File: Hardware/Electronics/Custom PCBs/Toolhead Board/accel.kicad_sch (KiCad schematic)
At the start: 1 part, among them U10 BMI270

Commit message: Remove locks
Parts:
- added C49: 100n, symbol Device:C
- added JP2: SolderJumper_3_Bridged123, symbol Jumper:SolderJumper_3_Bridged123
- added JP3: SolderJumper_2_Open, symbol Jumper:SolderJumper_2_Open
- added R39, R40: 2.2k, symbol Device:R
- added R41: 10k, symbol Device:R
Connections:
- net Address Selection: now reaches U10.1 (SDO)
- net Address Selection: now also JP3.2 (B), R41.1
- net SCL: now reaches U10.13 (SCX)
- net SCL: now also R39.2
- net SDA: now reaches U10.14 (SDX)
- net SDA: now also R40.2
- net +3.3V: now reaches U10.5 (VDDIO)
- net +3.3V: now also U10.8 (VDD), C49.1, JP2.2 (C), JP3.1 (A)
- net GND: now reaches U10.6 (GNDIO)
- net GND: now also U10.7 (GND), C49.2, R41.2
- new net: JP2.1 (A), R39.1
- new net: JP2.3 (B), R40.1
- no-connect marks 0 -> 7
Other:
- moved on the sheet: U10

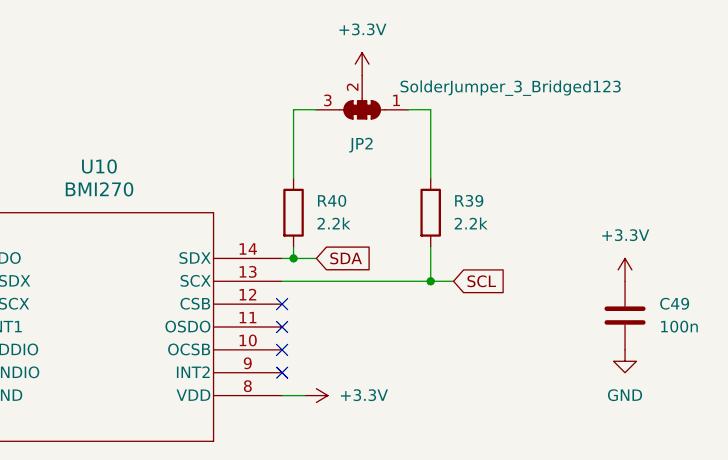
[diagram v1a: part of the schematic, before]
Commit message: Finish Toolhead Schematic
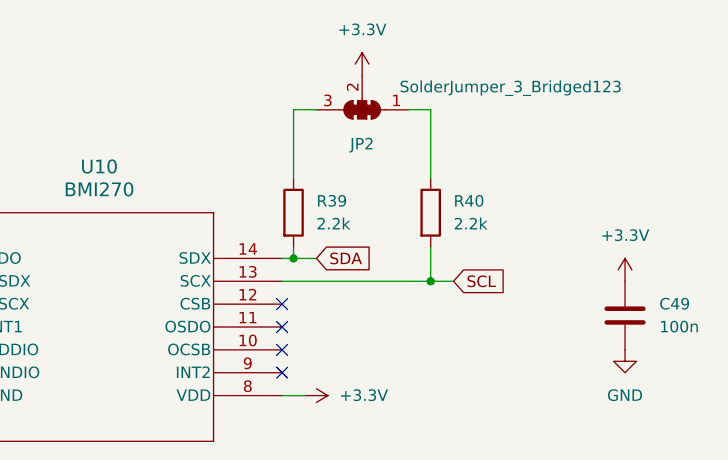
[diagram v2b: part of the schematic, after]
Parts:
- C49: Digikey (none) -> 1276-1935-1-ND
- R39: renamed from R40; footprint (none) -> Resistor_SMD:R_0603_1608Metric_Pad0.98x0.95mm_HandSolder; Digikey (none) -> 1292-WR06X103JTLCT-ND
- R40: renamed from R39; footprint (none) -> Resistor_SMD:R_0603_1608Metric_Pad0.98x0.95mm_HandSolder; Digikey (none) -> 1292-WR06X103JTLCT-ND
- R41: footprint (none) -> Resistor_SMD:R_0603_1608Metric_Pad0.98x0.95mm_HandSolder; Digikey (none) -> 1292-WR06X103JTLCT-ND
- U10: Digikey (none) -> 828-1091-1-ND
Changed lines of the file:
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@@
   (symbol (lib_id "power:GND") (at 59.69 58.42 270) (unit 1)
     (in_bom yes) (on_board yes) (dnp no) (fields_autoplaced)
-    (property "Reference" "#PWR074" (at 53.34 58.42 0)
+    (property "Reference" "#PWR099" (at 53.34 58.42 0)
       (effects (font (size 1.27 1.27)) hide)
     )
@@
       (project "Toolhead Board"
         (path "/a1747683-152e-4245-ab61-2d33ce6021ef/7be2b1b8-8861-4283-9878-3fb2e6cb9107"
-          (reference "#PWR074") (unit 1)
+          (reference "#PWR099") (unit 1)
         )
       )
@@
       (effects (font (size 1.27 1.27)) hide)
     )
+    (property "Digikey" "1276-1935-1-ND" (at 140.97 49.53 0)
+      (effects (font (size 1.27 1.27)) hide)
+    )
     (pin "1")
     (pin "2")
@@
     (property "Datasheet" "BMI270" (at 62.23 43.18 0)
       (effects (font (size 1.27 1.27) italic) hide)
+    )
+    (property "Digikey" "828-1091-1-ND" (at 62.23 43.18 0)
+      (effects (font (size 1.27 1.27)) hide)
     )
     (pin "1")
@@
     (pin "4")
     (pin "5")
+    (pin "8")
+    (pin "9")
     (pin "6")
     (pin "7")
-    (pin "8")
-    (pin "9")
     (instances
       (project "Toolhead Board"
@@
   (symbol (lib_id "Device:R") (at 119.38 38.1 0) (unit 1)
     (in_bom yes) (on_board yes) (dnp no) (fields_autoplaced)
-    (property "Reference" "R39" (at 121.92 36.83 0)
+    (property "Reference" "R40" (at 121.92 36.83 0)
       (effects (font (size 1.27 1.27)) (justify left))
     )
@@
       (effects (font (size 1.27 1.27)) (justify left))
     )
-    (property "Footprint" "" (at 117.602 38.1 90)
+    (property "Footprint" "Resistor_SMD:R_0603_1608Metric_Pad0.98x0.95mm_HandSolder" (at 117.602 38.1 90)
       (effects (font (size 1.27 1.27)) hide)
     )
@@
       (effects (font (size 1.27 1.27)) hide)
     )
-    (pin "1")
-    (pin "2")
-    (instances
-      (project "Toolhead Board"
-        (path "/a1747683-152e-4245-ab61-2d33ce6021ef/7be2b1b8-8861-4283-9878-3fb2e6cb9107"
-          (reference "R39") (unit 1)
+    (property "Digikey" "1292-WR06X103JTLCT-ND" (at 119.38 38.1 0)
+      (effects (font (size 1.27 1.27)) hide)
+    )
+    (pin "1")
+    (pin "2")
+    (instances
+      (project "Toolhead Board"
+        (path "/a1747683-152e-4245-ab61-2d33ce6021ef/7be2b1b8-8861-4283-9878-3fb2e6cb9107"
+          (reference "R40") (unit 1)
         )
       )
@@
   (symbol (lib_id "power:+3.3V") (at 41.91 35.56 0) (unit 1)
     (in_bom yes) (on_board yes) (dnp no) (fields_autoplaced)
-    (property "Reference" "#PWR079" (at 41.91 39.37 0)
+    (property "Reference" "#PWR094" (at 41.91 39.37 0)
       (effects (font (size 1.27 1.27)) hide)
     )
@@
       (project "Toolhead Board"
         (path "/a1747683-152e-4245-ab61-2d33ce6021ef/7be2b1b8-8861-4283-9878-3fb2e6cb9107"
-          (reference "#PWR079") (unit 1)
+          (reference "#PWR094") (unit 1)
         )
       )
@@
       (effects (font (size 1.27 1.27)) (justify left))
     )
-    (property "Footprint" "" (at 43.688 46.99 90)
+    (property "Footprint" "Resistor_SMD:R_0603_1608Metric_Pad0.98x0.95mm_HandSolder" (at 43.688 46.99 90)
       (effects (font (size 1.27 1.27)) hide)
     )
@@
       (effects (font (size 1.27 1.27)) hide)
     )
+    (property "Digikey" "1292-WR06X103JTLCT-ND" (at 41.91 46.99 0)
+      (effects (font (size 1.27 1.27)) hide)
+    )
     (pin "1")
     (pin "2")
@@
   (symbol (lib_id "power:+3.3V") (at 140.97 45.72 0) (unit 1)
     (in_bom yes) (on_board yes) (dnp no) (fields_autoplaced)
-    (property "Reference" "#PWR077" (at 140.97 49.53 0)
+    (property "Reference" "#PWR095" (at 140.97 49.53 0)
       (effects (font (size 1.27 1.27)) hide)
     )
@@
       (project "Toolhead Board"
         (path "/a1747683-152e-4245-ab61-2d33ce6021ef/7be2b1b8-8861-4283-9878-3fb2e6cb9107"
-          (reference "#PWR077") (unit 1)
+          (reference "#PWR095") (unit 1)
         )
       )
@@
   (symbol (lib_id "power:+3.3V") (at 105.41 58.42 270) (unit 1)
     (in_bom yes) (on_board yes) (dnp no) (fields_autoplaced)
-    (property "Reference" "#PWR076" (at 101.6 58.42 0)
+    (property "Reference" "#PWR0100" (at 101.6 58.42 0)
       (effects (font (size 1.27 1.27)) hide)
     )
@@
       (project "Toolhead Board"
         (path "/a1747683-152e-4245-ab61-2d33ce6021ef/7be2b1b8-8861-4283-9878-3fb2e6cb9107"
-          (reference "#PWR076") (unit 1)
+          (reference "#PWR0100") (unit 1)
         )
       )
@@
   (symbol (lib_id "power:+3.3V") (at 59.69 53.34 90) (unit 1)
     (in_bom yes) (on_board yes) (dnp no) (fields_autoplaced)
-    (property "Reference" "#PWR075" (at 63.5 53.34 0)
+    (property "Reference" "#PWR097" (at 63.5 53.34 0)
       (effects (font (size 1.27 1.27)) hide)
     )
@@
       (project "Toolhead Board"
         (path "/a1747683-152e-4245-ab61-2d33ce6021ef/7be2b1b8-8861-4283-9878-3fb2e6cb9107"
-          (reference "#PWR075") (unit 1)
+          (reference "#PWR097") (unit 1)
         )
       )
@@
   (symbol (lib_id "power:GND") (at 41.91 50.8 0) (unit 1)
     (in_bom yes) (on_board yes) (dnp no) (fields_autoplaced)
-    (property "Reference" "#PWR080" (at 41.91 57.15 0)
+    (property "Reference" "#PWR096" (at 41.91 57.15 0)
       (effects (font (size 1.27 1.27)) hide)
     )
@@
       (project "Toolhead Board"
         (path "/a1747683-152e-4245-ab61-2d33ce6021ef/7be2b1b8-8861-4283-9878-3fb2e6cb9107"
-          (reference "#PWR080") (unit 1)
+          (reference "#PWR096") (unit 1)
         )
       )
@@
   (symbol (lib_id "Device:R") (at 104.14 38.1 0) (unit 1)
     (in_bom yes) (on_board yes) (dnp no) (fields_autoplaced)
-    (property "Reference" "R40" (at 106.68 36.83 0)
+    (property "Reference" "R39" (at 106.68 36.83 0)
       (effects (font (size 1.27 1.27)) (justify left))
     )
@@
       (effects (font (size 1.27 1.27)) (justify left))
     )
-    (property "Footprint" "" (at 102.362 38.1 90)
+    (property "Footprint" "Resistor_SMD:R_0603_1608Metric_Pad0.98x0.95mm_HandSolder" (at 102.362 38.1 90)
       (effects (font (size 1.27 1.27)) hide)
     )
@@
       (effects (font (size 1.27 1.27)) hide)
     )
-    (pin "1")
-    (pin "2")
-    (instances
-      (project "Toolhead Board"
-        (path "/a1747683-152e-4245-ab61-2d33ce6021ef/7be2b1b8-8861-4283-9878-3fb2e6cb9107"
-          (reference "R40") (unit 1)
+    (property "Digikey" "1292-WR06X103JTLCT-ND" (at 104.14 38.1 0)
+      (effects (font (size 1.27 1.27)) hide)
+    )
+    (pin "1")
+    (pin "2")
+    (instances
+      (project "Toolhead Board"
+        (path "/a1747683-152e-4245-ab61-2d33ce6021ef/7be2b1b8-8861-4283-9878-3fb2e6cb9107"
+          (reference "R39") (unit 1)
         )
       )
@@
   (symbol (lib_id "power:GND") (at 140.97 53.34 0) (unit 1)
     (in_bom yes) (on_board yes) (dnp no) (fields_autoplaced)
-    (property "Reference" "#PWR078" (at 140.97 59.69 0)
+    (property "Reference" "#PWR098" (at 140.97 59.69 0)
       (effects (font (size 1.27 1.27)) hide)
     )
@@
       (project "Toolhead Board"
         (path "/a1747683-152e-4245-ab61-2d33ce6021ef/7be2b1b8-8861-4283-9878-3fb2e6cb9107"
-          (reference "#PWR078") (unit 1)
+          (reference "#PWR098") (unit 1)
         )
       )
@@
   (symbol (lib_id "power:+3.3V") (at 111.76 22.86 0) (unit 1)
     (in_bom yes) (on_board yes) (dnp no) (fields_autoplaced)
-    (property "Reference" "#PWR073" (at 111.76 26.67 0)
+    (property "Reference" "#PWR093" (at 111.76 26.67 0)
       (effects (font (size 1.27 1.27)) hide)
     )
@@
       (project "Toolhead Board"
         (path "/a1747683-152e-4245-ab61-2d33ce6021ef/7be2b1b8-8861-4283-9878-3fb2e6cb9107"
-          (reference "#PWR073") (unit 1)
-        )
-      )
+          (reference "#PWR093") (unit 1)
+        )
+      )

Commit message: Continue adding footprints
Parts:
- C49: footprint (none) -> Capacitor_SMD:C_0603_1608Metric_Pad1.08x0.95mm_HandSolder
- JP2: footprint (none) -> Jumper:SolderJumper-3_P1.3mm_Open_RoundedPad1.0x1.5mm
- JP3: footprint (none) -> Jumper:SolderJumper-2_P1.3mm_Open_RoundedPad1.0x1.5mm
- U10: footprint BMI270_BOS -> Package_LGA:Bosch_LGA-14_3x2.5mm_P0.5mm
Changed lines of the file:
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@@
 			)
 		)
-		(property "Footprint" ""
+		(property "Footprint" "Jumper:SolderJumper-3_P1.3mm_Open_RoundedPad1.0x1.5mm"
 			(at 111.76 26.67 0)
 			(effects
@@
 			)
 		)
-		(property "Footprint" ""
+		(property "Footprint" "Jumper:SolderJumper-2_P1.3mm_Open_RoundedPad1.0x1.5mm"
 			(at 41.91 39.37 0)
 			(effects
@@
 			)
 		)
-		(property "Footprint" ""
+		(property "Footprint" "Capacitor_SMD:C_0603_1608Metric_Pad1.08x0.95mm_HandSolder"
 			(at 141.9352 53.34 0)
 			(effects
@@
 			)
 		)
-		(property "Footprint" "BMI270_BOS"
+		(property "Footprint" "Package_LGA:Bosch_LGA-14_3x2.5mm_P0.5mm"
 			(at 62.23 43.18 0)
 			(effects

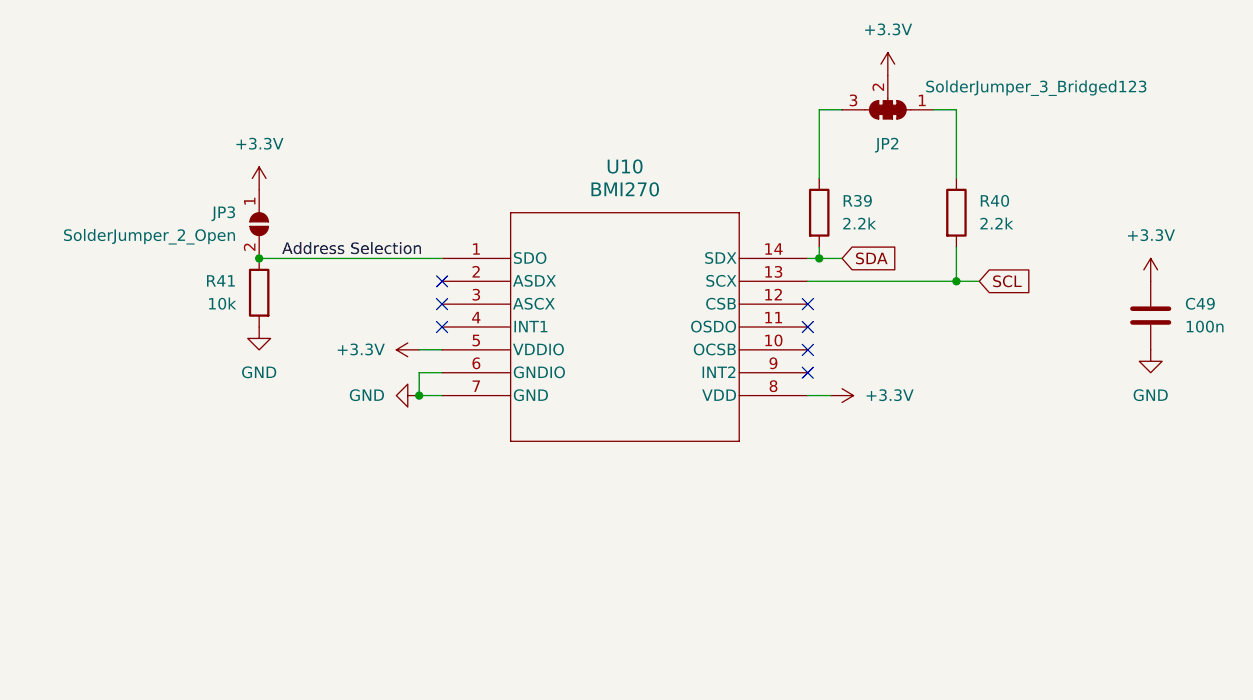
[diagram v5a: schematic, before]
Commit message: Update toolhead schematic+layout and add tolerances to base
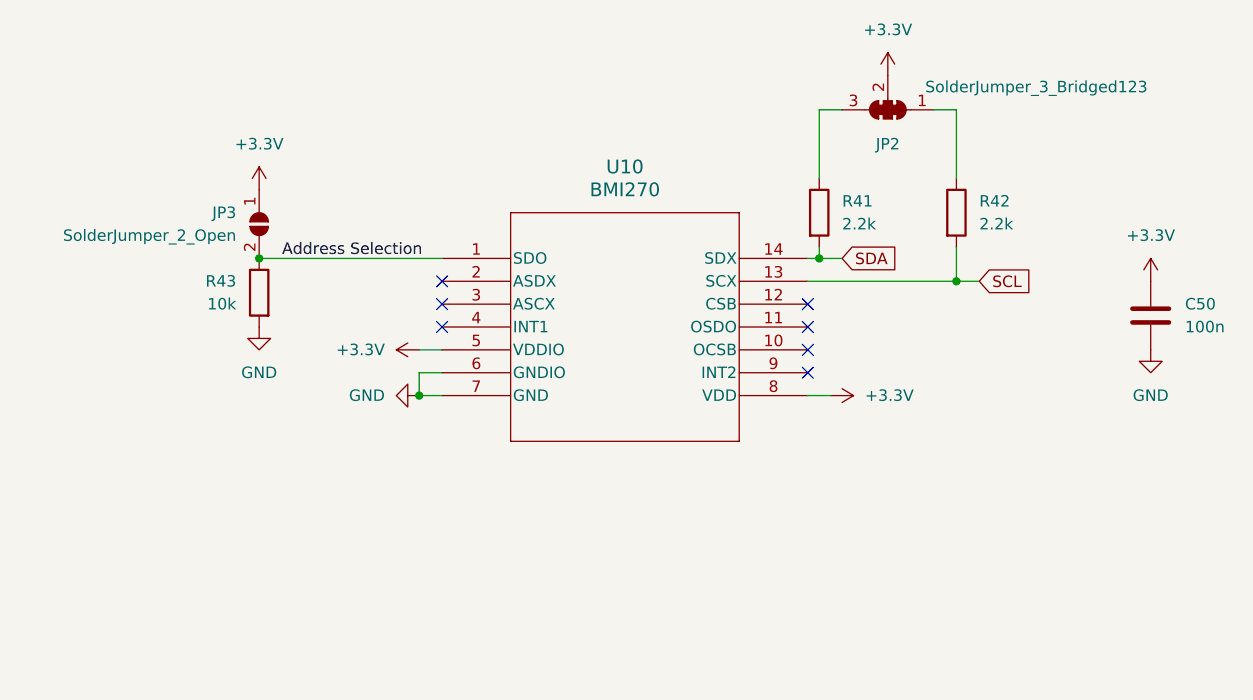
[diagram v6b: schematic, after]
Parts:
- renumbered C49 to C50, R39 to R41, R40 to R42, R41 to R43
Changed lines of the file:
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@@
 		(dnp no)
 		(fields_autoplaced yes)
-		(property "Reference" "#PWR098"
+		(property "Reference" "#PWR0100"
 			(at 53.34 58.42 0)
 			(effects
@@
 			(project "Toolhead Board"
 				(path "/a1747683-152e-4245-ab61-2d33ce6021ef/7be2b1b8-8861-4283-9878-3fb2e6cb9107"
-					(reference "#PWR098")
+					(reference "#PWR0100")
 					(unit 1)
 				)
@@
 		(dnp no)
 		(fields_autoplaced yes)
-		(property "Reference" "C49"
+		(property "Reference" "C50"
 			(at 144.78 48.26 0)
 			(effects
@@
 			(project "Toolhead Board"
 				(path "/a1747683-152e-4245-ab61-2d33ce6021ef/7be2b1b8-8861-4283-9878-3fb2e6cb9107"
-					(reference "C49")
+					(reference "C50")
 					(unit 1)
 				)
@@
 		(dnp no)
 		(fields_autoplaced yes)
-		(property "Reference" "R40"
+		(property "Reference" "R42"
 			(at 121.92 36.83 0)
 			(effects
@@
 			(project "Toolhead Board"
 				(path "/a1747683-152e-4245-ab61-2d33ce6021ef/7be2b1b8-8861-4283-9878-3fb2e6cb9107"
-					(reference "R40")
+					(reference "R42")
 					(unit 1)
 				)
@@
 		(dnp no)
 		(fields_autoplaced yes)
-		(property "Reference" "#PWR093"
+		(property "Reference" "#PWR095"
 			(at 41.91 39.37 0)
 			(effects
@@
 			(project "Toolhead Board"
 				(path "/a1747683-152e-4245-ab61-2d33ce6021ef/7be2b1b8-8861-4283-9878-3fb2e6cb9107"
-					(reference "#PWR093")
+					(reference "#PWR095")
 					(unit 1)
 				)
@@
 		(on_board yes)
 		(dnp no)
-		(property "Reference" "R41"
+		(property "Reference" "R43"
 			(at 39.37 45.72 0)
 			(effects
@@
 			(project "Toolhead Board"
 				(path "/a1747683-152e-4245-ab61-2d33ce6021ef/7be2b1b8-8861-4283-9878-3fb2e6cb9107"
-					(reference "R41")
+					(reference "R43")
 					(unit 1)
 				)
@@
 		(dnp no)
 		(fields_autoplaced yes)
-		(property "Reference" "#PWR094"
+		(property "Reference" "#PWR096"
 			(at 140.97 49.53 0)
 			(effects
@@
 			(project "Toolhead Board"
 				(path "/a1747683-152e-4245-ab61-2d33ce6021ef/7be2b1b8-8861-4283-9878-3fb2e6cb9107"
-					(reference "#PWR094")
+					(reference "#PWR096")
 					(unit 1)
 				)
@@
 		(dnp no)
 		(fields_autoplaced yes)
-		(property "Reference" "#PWR099"
+		(property "Reference" "#PWR0101"
 			(at 101.6 58.42 0)
 			(effects
@@
 			(project "Toolhead Board"
 				(path "/a1747683-152e-4245-ab61-2d33ce6021ef/7be2b1b8-8861-4283-9878-3fb2e6cb9107"
-					(reference "#PWR099")
+					(reference "#PWR0101")
 					(unit 1)
 				)
@@
 		(dnp no)
 		(fields_autoplaced yes)
-		(property "Reference" "#PWR096"
+		(property "Reference" "#PWR098"
 			(at 63.5 53.34 0)
 			(effects
@@
 			(project "Toolhead Board"
 				(path "/a1747683-152e-4245-ab61-2d33ce6021ef/7be2b1b8-8861-4283-9878-3fb2e6cb9107"
-					(reference "#PWR096")
+					(reference "#PWR098")
 					(unit 1)
 				)
@@
 		(dnp no)
 		(fields_autoplaced yes)
-		(property "Reference" "#PWR095"
+		(property "Reference" "#PWR097"
 			(at 41.91 57.15 0)
 			(effects
@@
 			(project "Toolhead Board"
 				(path "/a1747683-152e-4245-ab61-2d33ce6021ef/7be2b1b8-8861-4283-9878-3fb2e6cb9107"
-					(reference "#PWR095")
+					(reference "#PWR097")
 					(unit 1)
 				)
@@
 		(dnp no)
 		(fields_autoplaced yes)
-		(property "Reference" "R39"
+		(property "Reference" "R41"
 			(at 106.68 36.83 0)
 			(effects
@@
 			(project "Toolhead Board"
 				(path "/a1747683-152e-4245-ab61-2d33ce6021ef/7be2b1b8-8861-4283-9878-3fb2e6cb9107"
-					(reference "R39")
+					(reference "R41")
 					(unit 1)
 				)
@@
 		(dnp no)
 		(fields_autoplaced yes)
-		(property "Reference" "#PWR097"
+		(property "Reference" "#PWR099"
 			(at 140.97 59.69 0)
 			(effects
@@
 			(project "Toolhead Board"
 				(path "/a1747683-152e-4245-ab61-2d33ce6021ef/7be2b1b8-8861-4283-9878-3fb2e6cb9107"
-					(reference "#PWR097")
+					(reference "#PWR099")
 					(unit 1)
 				)
@@
 		(dnp no)
 		(fields_autoplaced yes)
-		(property "Reference" "#PWR092"
+		(property "Reference" "#PWR094"
 			(at 111.76 26.67 0)
 			(effects
@@
 			(project "Toolhead Board"
 				(path "/a1747683-152e-4245-ab61-2d33ce6021ef/7be2b1b8-8861-4283-9878-3fb2e6cb9107"
-					(reference "#PWR092")
-					(unit 1)
-				)
+					(reference "#PWR094")
+					(unit 1)
+				)
